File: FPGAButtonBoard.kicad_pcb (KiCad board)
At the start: 2 copper layers, 58 parts, among them J1 Conn_02x20_Odd_Even, J2 Analog Discovery 2, SW1 SW_DIP_x08, SW2 SW_DIP_x08, SW3 SW_Push, SW4 SW_Push, SW5 SW_Push, SW6 SW_Push, SW7 SW_Push, SW8 SW_SPST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

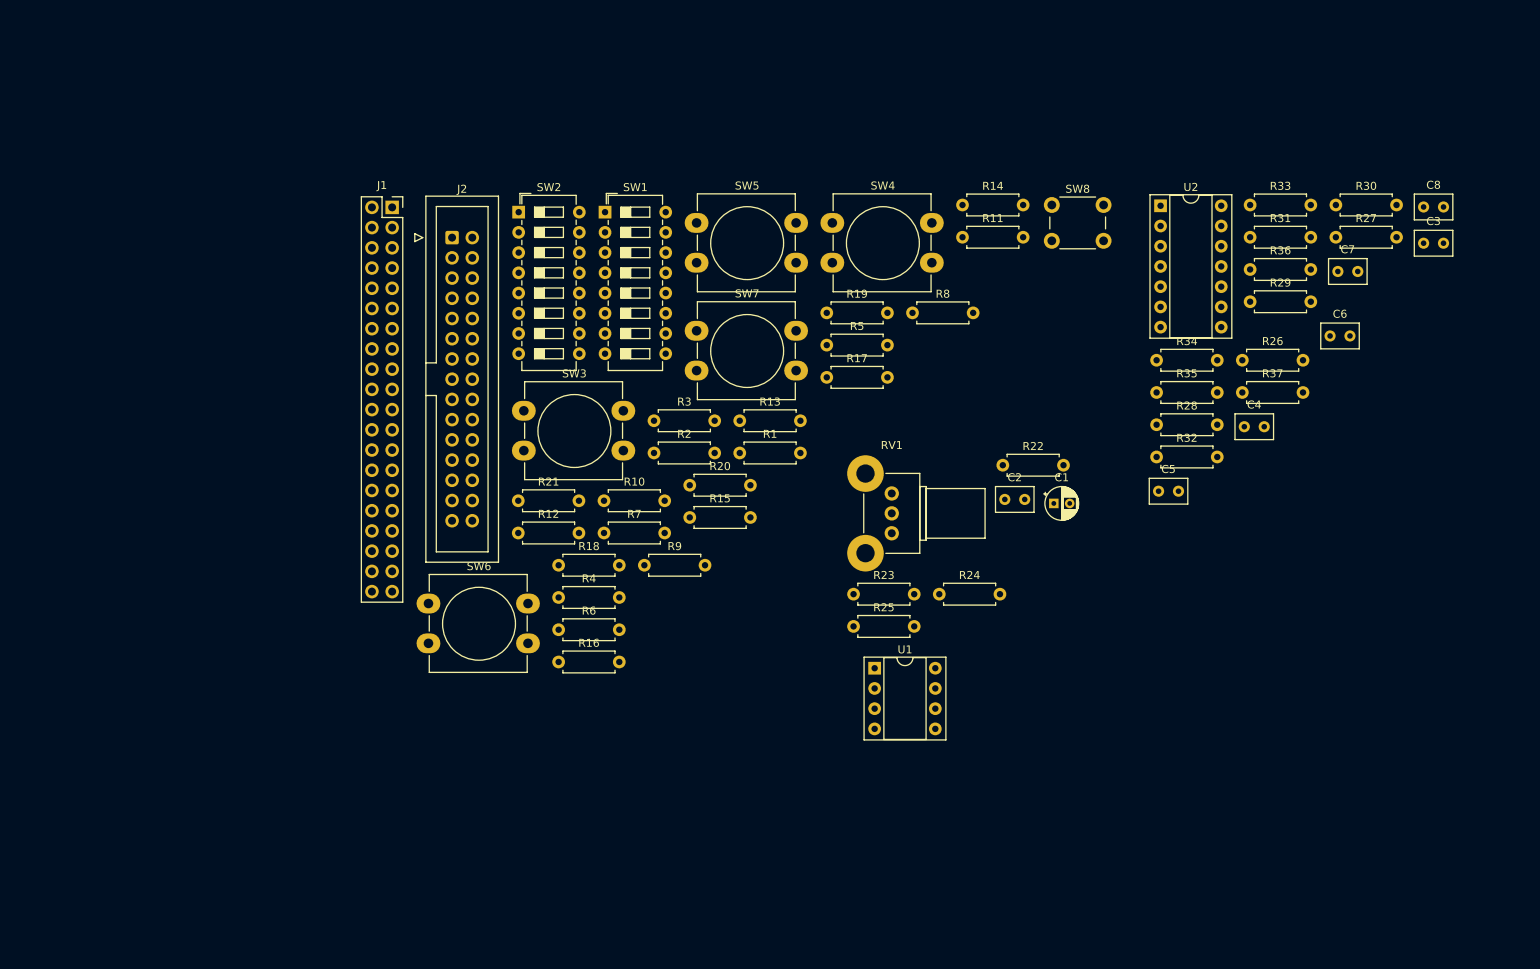
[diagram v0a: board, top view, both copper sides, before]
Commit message: Adicionado os furos de montagem. Definidos os footprints
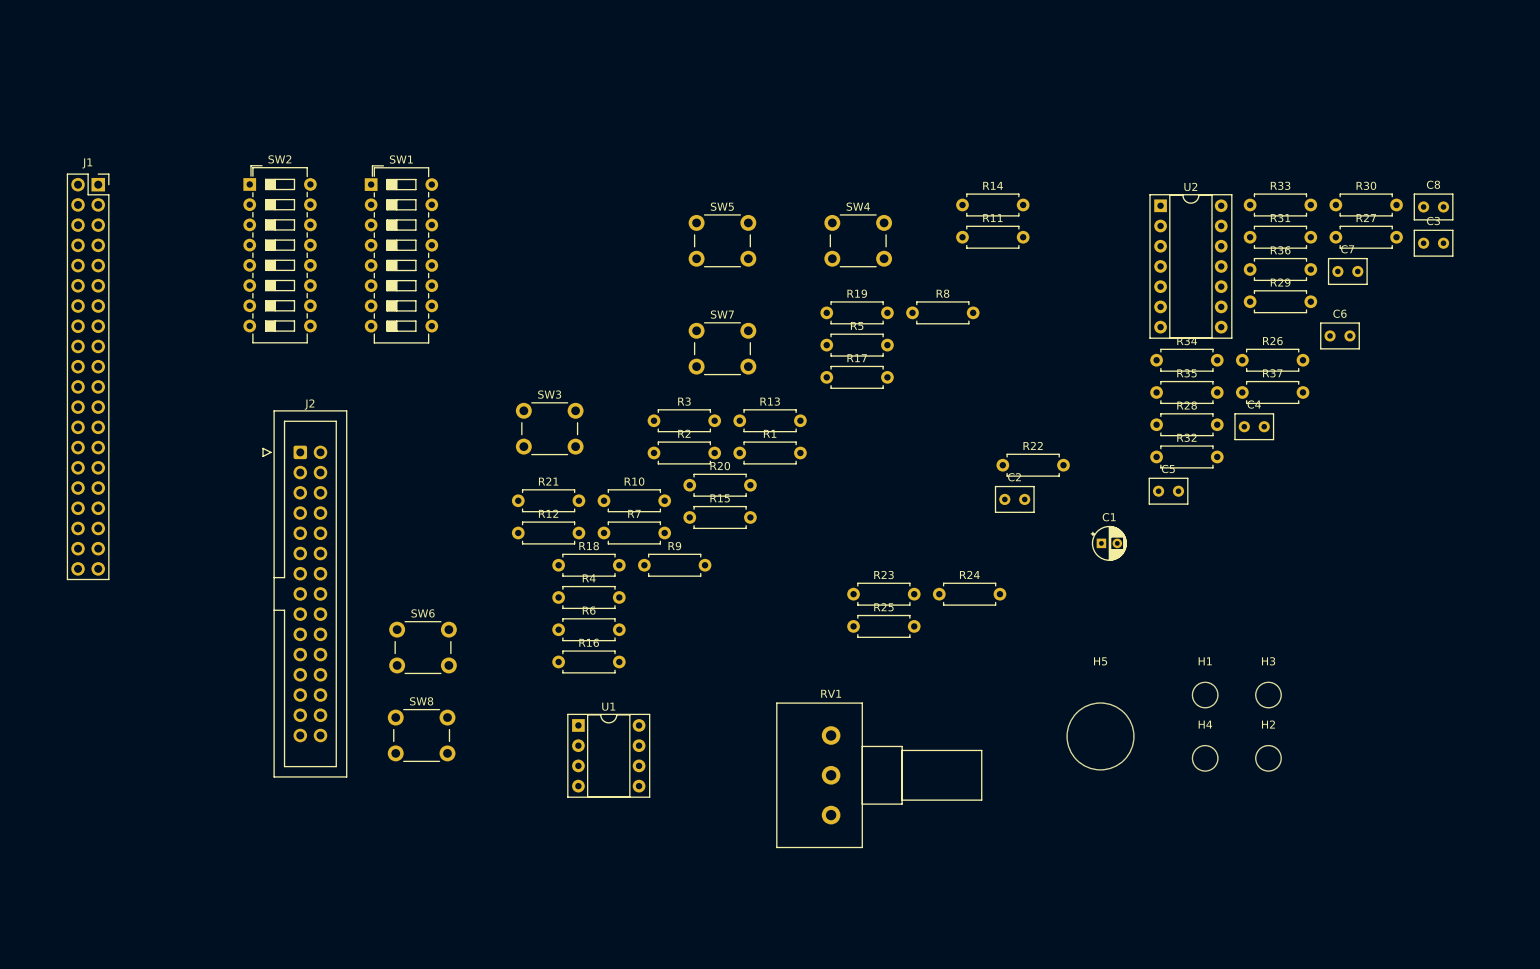
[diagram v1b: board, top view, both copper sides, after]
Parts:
- added H1: MountingHole, MountingHole:MountingHole_3.2mm_M3, F.Cu at (176.5, 106.0)
- added H2: MountingHole, MountingHole:MountingHole_3.2mm_M3, F.Cu at (184.5, 114.0)
- added H3: MountingHole, MountingHole:MountingHole_3.2mm_M3, F.Cu at (184.5, 106.0)
- added H4: MountingHole, MountingHole:MountingHole_3.2mm_M3, F.Cu at (176.5, 114.0)
- added H5: Potentiometer Hole, MountingHole:MountingHole_8.4mm_M8, F.Cu at (163.4, 111.2)
- RV1: footprint Potentiometer_THT:Potentiometer_Alps_RK09K_Single_Horizontal -> Potentiometer_THT:Potentiometer_Alps_RK163_Single_Horizontal
- SW3, SW4, SW5, SW6, SW7: footprint Button_Switch_THT:SW_PUSH-12mm_Wuerth-430476085716 -> Button_Switch_THT:SW_PUSH_6mm
- moved SW8 104.6 mm to (74.9, 108.9)
- moved U1 37.9 mm to (97.8, 109.9)
- moved J1 37.0 mm to (37.5, 41.9)
- moved RV1 36.2 mm to (129.5, 121.1)
- moved SW2 34.0 mm to (56.5, 41.9)
- moved J2 33.0 mm to (62.9, 75.6)
- moved SW1 29.6 mm to (71.8, 41.9)
- moved C1 7.81 mm to (163.5, 87.0)
- moved SW6 5.12 mm to (75.0, 97.8)

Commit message: Organizado os componentes na placa.
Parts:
- J1: moved to B.Cu
- moved H4 162.9 mm to (31.8, 39.4)
- moved H3 151.7 mm to (33.0, 97.2)
- moved C3 108.1 mm to (95.9, 47.6)
- moved R30 99.4 mm to (94.0, 54.0)
- moved R11 98.4 mm to (47.6, 47.0), turned to -90 degrees
- moved R5 94.0 mm to (36.2, 47.0), turned to -90 degrees
- moved R1 94.0 mm to (28.6, 47.0), turned to -90 degrees
- moved R26 87.4 mm to (94.0, 59.1)
- moved R27 86.9 mm to (106.7, 59.1)
- moved H5 84.8 mm to (80.6, 92.7)
- moved SW8 81.2 mm to (154.8, 94.9)
- moved J1 79.5 mm to (114.3, 21.6), turned to 90 degrees
- moved R3 78.8 mm to (32.4, 47.0), turned to -90 degrees
- moved C4 76.9 mm to (108.6, 47.6)
- moved R31 76.3 mm to (106.0, 54.0)
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
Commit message: Definida a borda da placa.
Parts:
- moved SW3 87.2 mm to (172.6, 101.3)
- moved R26 86.6 mm to (172.1, 96.5)
- moved R30 86.6 mm to (172.1, 91.4)
- moved C3 86.6 mm to (174.0, 85.1)
- moved R31 86.0 mm to (183.4, 91.4)
- moved C4 85.4 mm to (185.4, 85.1)
- moved R27 85.4 mm to (183.4, 96.5)
- moved SW4 85.4 mm to (184.0, 101.3)
- moved C5 84.9 mm to (196.9, 85.1)
- moved R28 84.9 mm to (194.9, 96.5)
- moved R32 84.9 mm to (194.9, 91.4)
- moved SW5 84.9 mm to (195.5, 101.3)
- moved C6 84.3 mm to (208.3, 85.1)
- moved R29 84.3 mm to (206.4, 96.5)
- moved R33 84.3 mm to (206.4, 91.4)
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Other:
- board outline added: 134 x 83.2 mm

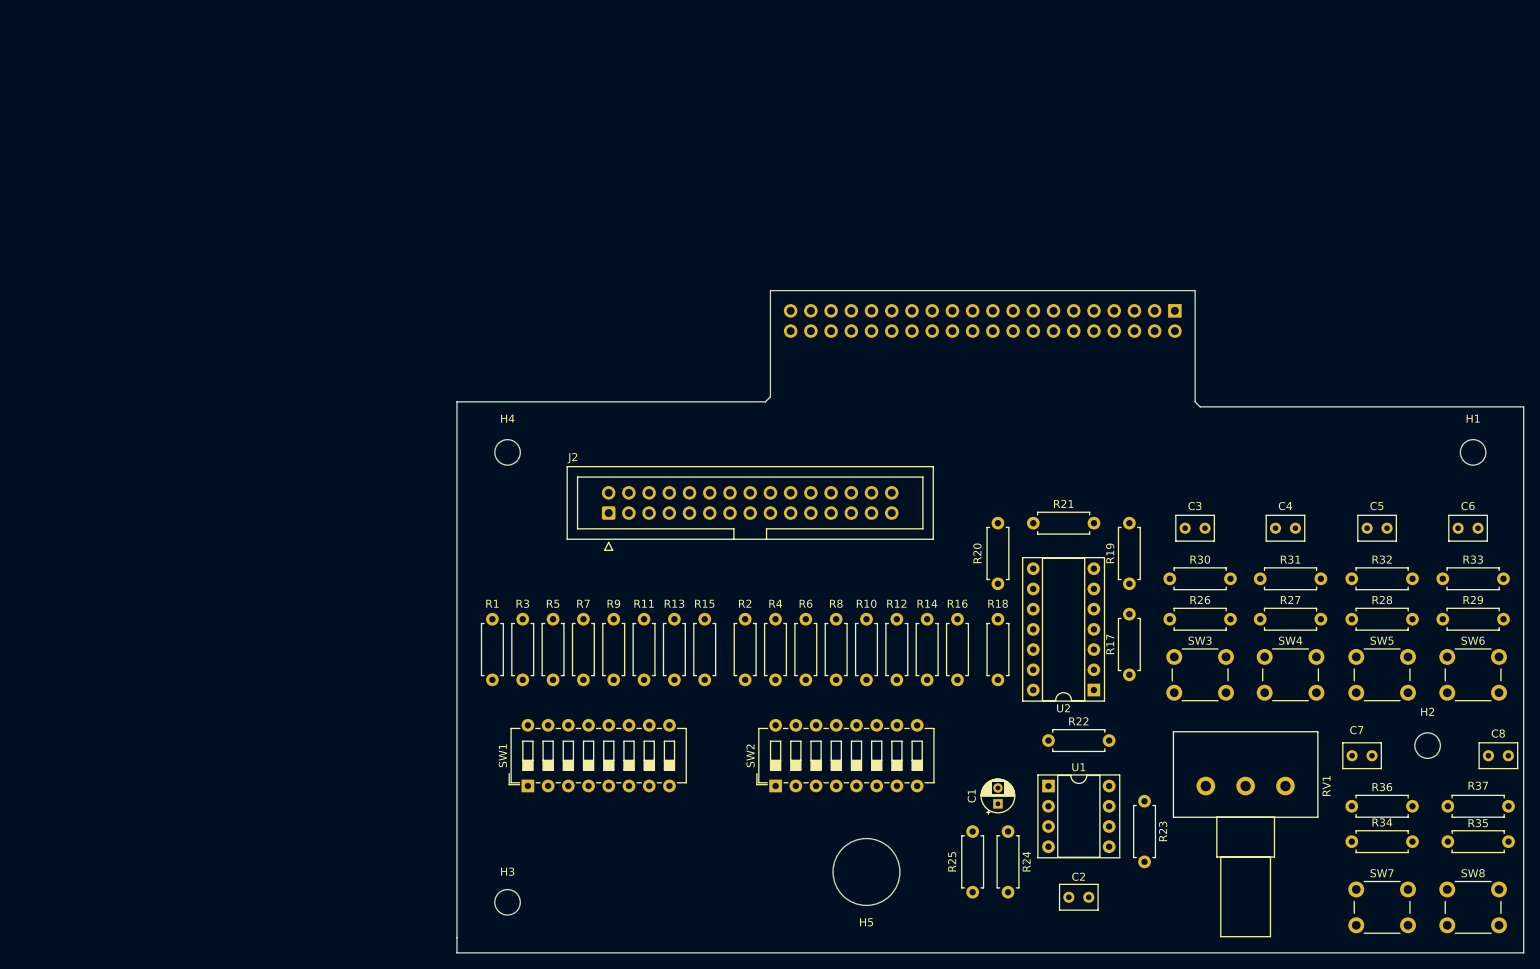
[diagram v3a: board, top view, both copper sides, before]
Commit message: Corrigido o footprint dos capacitores. Adicionado um capacitor de bypass. Adicionado o ground plane e logo.
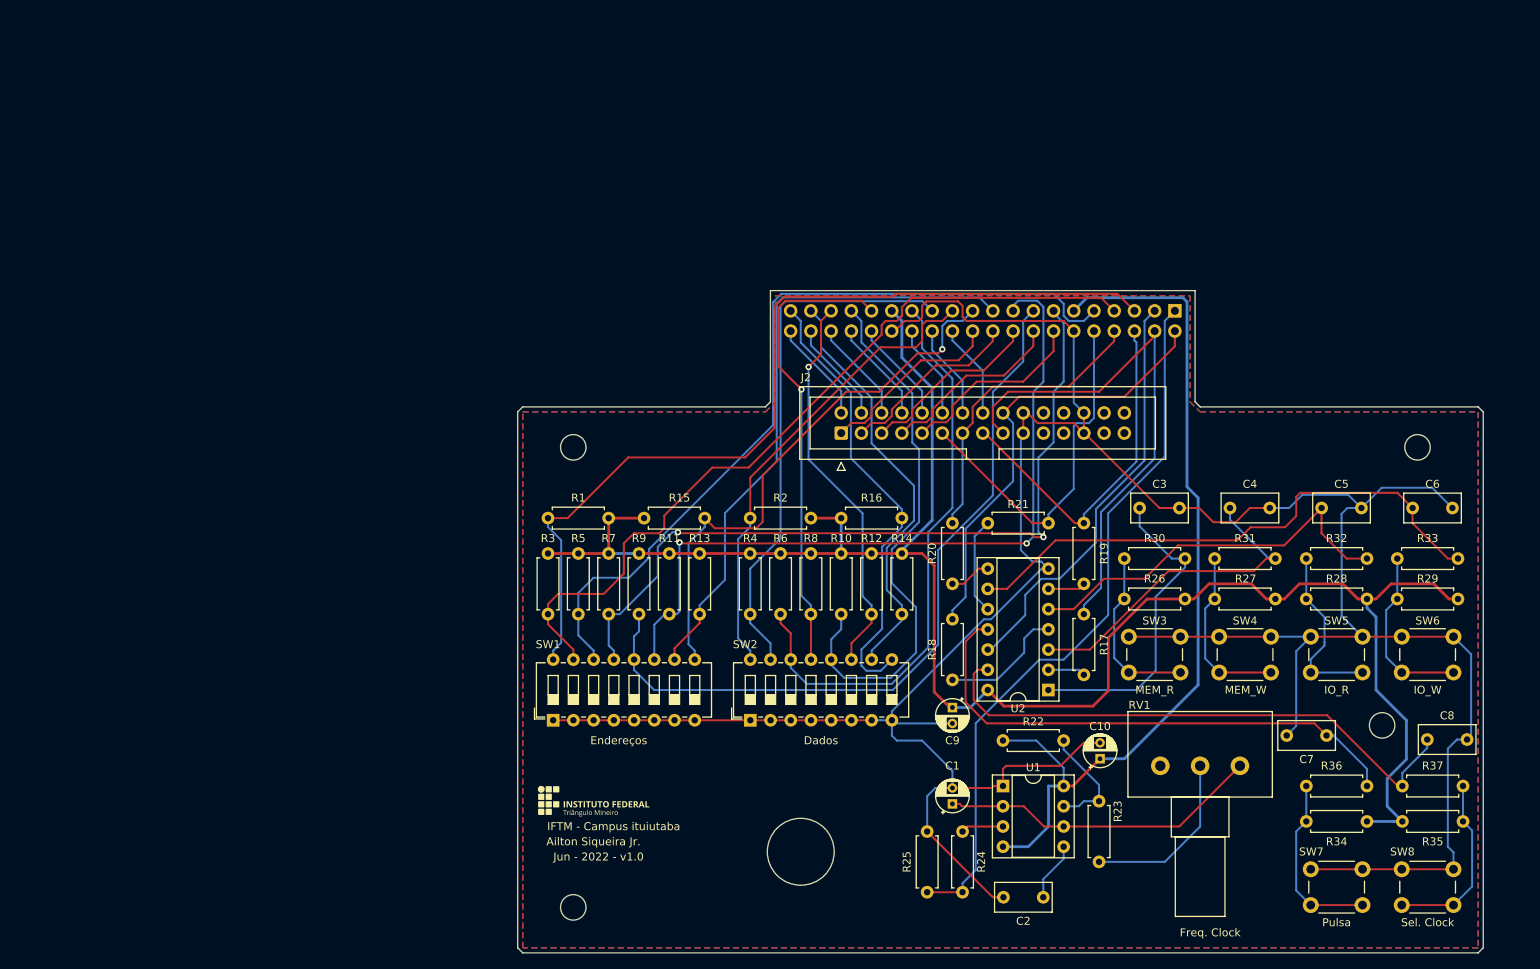
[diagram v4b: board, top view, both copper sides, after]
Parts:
- added C10: 10uF, Capacitor_THT:CP_Radial_D4.0mm_P2.00mm, F.Cu at (163.3, 114.0)
- added C9: 10uF, Capacitor_THT:CP_Radial_D4.0mm_P2.00mm, F.Cu at (144.8, 107.6)
- added G***: LOGO, Logo:IFTMLogoHor, F.Cu at (99.7, 119.4)
- C1: value 1uF -> 10uF
- C2, C3, C4, C5, C6, C7, C8: footprint Capacitor_THT:C_Rect_L4.6mm_W3.0mm_P2.50mm_MKS02_FKP02 -> Capacitor_THT:C_Rect_L7.0mm_W3.5mm_P5.00mm
- moved J2 30.9 mm to (130.8, 73.1)
- moved R1 19.4 mm to (101.6, 83.8), turned to 180 degrees
- moved R16 19.4 mm to (130.8, 83.8), turned to 0 degrees
- moved R2 15.1 mm to (127.0, 83.8), turned to 180 degrees
- moved R15 14.8 mm to (106.0, 83.8), turned to 0 degrees
- moved SW1 8.84 mm to (94.6, 109.2)
- moved SW2 8.84 mm to (119.4, 109.2)
- moved R10 8.84 mm to (130.8, 88.3)
- moved R4 8.84 mm to (119.4, 88.3)
- moved R5 8.84 mm to (97.8, 88.3)
- moved R8 8.84 mm to (127.0, 88.3)
- moved R11 8.84 mm to (109.2, 88.3)
- moved R13 8.84 mm to (113.0, 88.3)
- moved R3 8.84 mm to (94.0, 88.3)
- moved R6 8.84 mm to (123.2, 88.3)
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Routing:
- net GND: track 0.00 -> 385.9 mm
- net +3V3: track 0.00 -> 235.1 mm
- net Net-(J1-Pad5): track 0.00 -> 114.0 mm
- net +5V: track 0.00 -> 111.1 mm
- net Net-(J1-Pad9): track 0.00 -> 102.0 mm
- net Net-(J1-Pad7): track 0.00 -> 100.5 mm
- net Net-(J1-Pad13): track 0.00 -> 97.8 mm, vias 0 -> 2
- net Net-(J1-Pad17): track 0.00 -> 97.0 mm, vias 0 -> 2
- net Net-(J1-Pad15): track 0.00 -> 95.7 mm
- net /Clock/CLOCK_OUT: track 0.00 -> 90.3 mm
- net Net-(J1-Pad19): track 0.00 -> 78.2 mm
- net Net-(J1-Pad27): track 0.00 -> 72.9 mm
- net Net-(C8-Pad1): track 0.00 -> 70.7 mm
- net Net-(C6-Pad1): track 0.00 -> 70.0 mm
- net Net-(J1-Pad21): track 0.00 -> 69.6 mm, vias 0 -> 1
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- added copper zone on B.Cu, net GND
- added copper zone on F.Cu, net GND
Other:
- board size 134 x 83.2 mm -> 121.3 x 83.2 mm
- board text added: "Ailton Siqueira Jr."
- board text added: "Dados"
- board text added: "Endereços"
- board text added: "Freq. Clock"
- board text added: "IFTM - Campus ituiutaba"
- board text added: "IO_R"
- board text added: "IO_W"
- board text added: "Jun - 2022 - v1.0"
- board text added: "MEM_R"
- board text added: "MEM_W"
- board text added: "Pulsa"
- board text added: "Sel. Clock"

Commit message: Adicionados indicações dos elementos no silkscreen
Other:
- board text added: "Ajuste de Freq."
- board text added: "Clock"
- board text added: "Controle"
- board text added: "Dado"
- board text added: "Endereço"
- board text removed: "Dados"
- board text removed: "Endereços"
- board text removed: "Freq. Clock"
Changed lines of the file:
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@@
     )
   )
+  (gr_line (start 191.77 106.68) (end 210.185 106.68) (layer "F.SilkS") (width 0.15))
+  (gr_line (start 210.185 106.68) (end 210.185 95.885) (layer "F.SilkS") (width 0.15))
+  (gr_line (start 187.325 125.095) (end 210.185 125.095) (layer "F.SilkS") (width 0.15))
+  (gr_line (start 116.205 98.425) (end 140.335 98.425) (layer "F.SilkS") (width 0.15))
+  (gr_line (start 91.44 111.76) (end 98.425 111.76) (layer "F.SilkS") (width 0.15))
+  (gr_line (start 164.465 106.68) (end 184.15 106.68) (layer "F.SilkS") (width 0.15))
+  (gr_line (start 210.185 136.525) (end 201.295 136.525) (layer "F.SilkS") (width 0.15))
+  (gr_line (start 115.57 111.76) (end 115.57 98.425) (layer "F.SilkS") (width 0.15))
+  (gr_line (start 196.215 136.525) (end 187.325 136.525) (layer "F.SilkS") (width 0.15))
+  (gr_line (start 107.315 111.76) (end 115.57 111.76) (layer "F.SilkS") (width 0.15))
+  (gr_line (start 187.325 136.525) (end 187.325 125.095) (layer "F.SilkS") (width 0.15))
+  (gr_line (start 125.73 111.76) (end 116.205 111.76) (layer "F.SilkS") (width 0.15))
+  (gr_line (start 210.185 95.885) (end 164.465 95.885) (layer "F.SilkS") (width 0.15))
+  (gr_line (start 140.335 98.425) (end 140.335 111.76) (layer "F.SilkS") (width 0.15))
+  (gr_line (start 210.185 125.095) (end 210.185 136.525) (layer "F.SilkS") (width 0.15))
+  (gr_line (start 116.205 111.76) (end 116.205 98.425) (layer "F.SilkS") (width 0.15))
+  (gr_line (start 140.335 111.76) (end 130.81 111.76) (layer "F.SilkS") (width 0.15))
+  (gr_line (start 115.57 98.425) (end 91.44 98.425) (layer "F.SilkS") (width 0.15))
+  (gr_line (start 91.44 98.425) (end 91.44 111.76) (layer "F.SilkS") (width 0.15))
+  (gr_line (start 164.465 95.885) (end 164.465 106.68) (layer "F.SilkS") (width 0.15))
   (gr_line (start 210.82 69.85) (end 211.455 70.485) (layer "Edge.Cuts") (width 0.1))
   (gr_line (start 175.26 69.215) (end 175.895 69.85) (layer "Edge.Cuts") (width 0.1))
@@
   (gr_line (start 175.895 69.85) (end 210.82 69.85) (layer "Edge.Cuts") (width 0.1))
   (gr_line (start 211.455 70.485) (end 211.455 137.795) (layer "Edge.Cuts") (width 0.1))
+  (gr_text "Controle" (at 187.96 106.68) (layer "F.SilkS")
+    (effects (font (size 1 1) (thickness 0.15)))
+  )
   (gr_text "Sel. Clock" (at 204.47 134.62) (layer "F.SilkS")
     (effects (font (size 1 1) (thickness 0.15)))
@@
     (effects (font (size 1 1) (thickness 0.15)))
   )
-  (gr_text "Dados" (at 128.27 111.76) (layer "F.SilkS")
+  (gr_text "Clock" (at 198.755 136.525) (layer "F.SilkS")
+    (effects (font (size 1 1) (thickness 0.15)))
+  )
+  (gr_text "Dado" (at 128.27 111.76) (layer "F.SilkS")
     (effects (font (size 1 1) (thickness 0.15)))
   )
@@
     (effects (font (size 1 1) (thickness 0.15)))
   )
-  (gr_text "Freq. Clock" (at 177.165 135.89) (layer "F.SilkS")
+  (gr_text "Ajuste de Freq." (at 175.895 135.89) (layer "F.SilkS")
     (effects (font (size 1 1) (thickness 0.15)))
   )
@@
     (effects (font (size 1 1) (thickness 0.15)))
   )
-  (gr_text "Endereços" (at 102.87 111.76) (layer "F.SilkS")
+  (gr_text "Endereço" (at 102.87 111.76) (layer "F.SilkS")
     (effects (font (size 1 1) (thickness 0.15)))
   )
